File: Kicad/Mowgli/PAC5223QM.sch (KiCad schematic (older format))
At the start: 3 parts, among them J12 Serial, J16 SWD

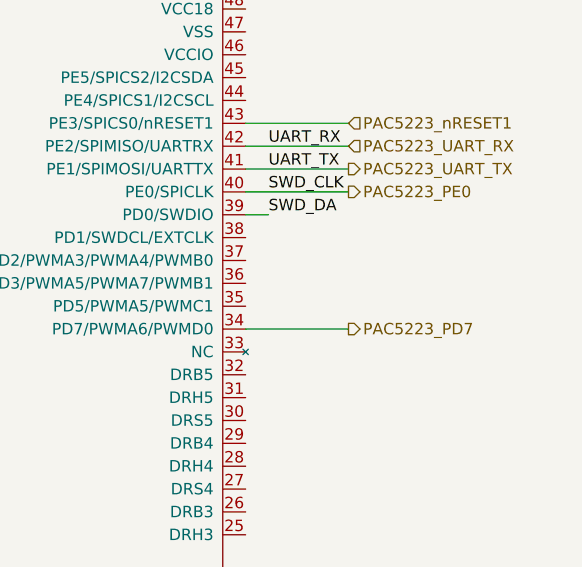
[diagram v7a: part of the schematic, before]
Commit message: reversed mechanical tilt and accelerometer circuit
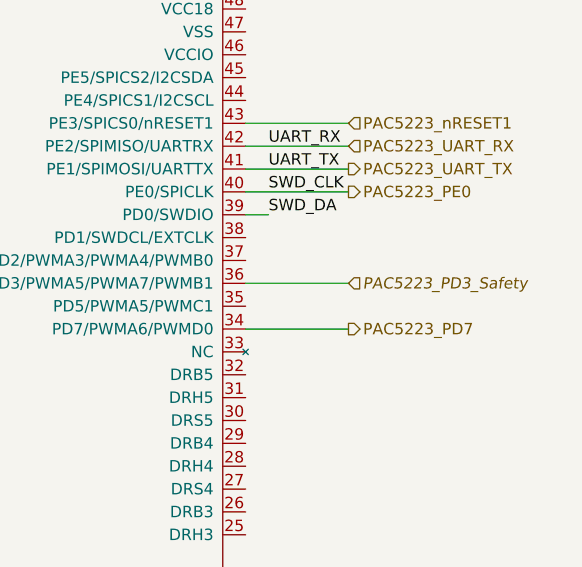
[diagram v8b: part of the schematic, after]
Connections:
- net PAC5223_PD3_Safety: now reaches U?.36 (PD3/PWMA5/PWMA7/PWMB1)
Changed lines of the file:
@@
 Wire Wire Line
 	7600 3800 7150 3800
+Text HLabel 7600 3600 2    49   Input Italic 0
+PAC5223_PD3_Safety
+Wire Wire Line
+	7600 3600 7150 3600
 $EndSCHEMATC
